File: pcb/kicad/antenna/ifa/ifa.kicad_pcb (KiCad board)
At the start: 2 copper layers, 27.6 x 86.4 mm, 1 part, among them P1 CONN_01X02

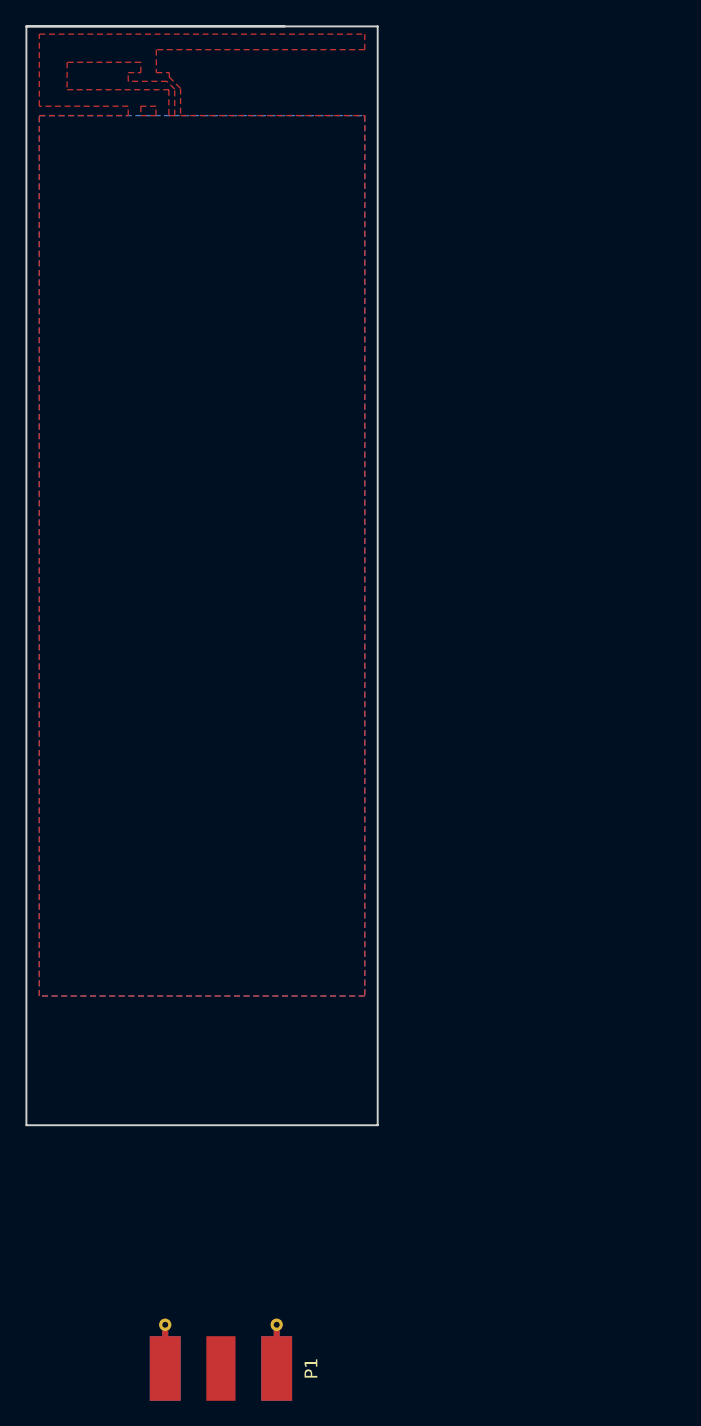
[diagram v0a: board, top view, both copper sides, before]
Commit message: Add second half of initial IFA design
Vias, drills, and padding still need to be configured.
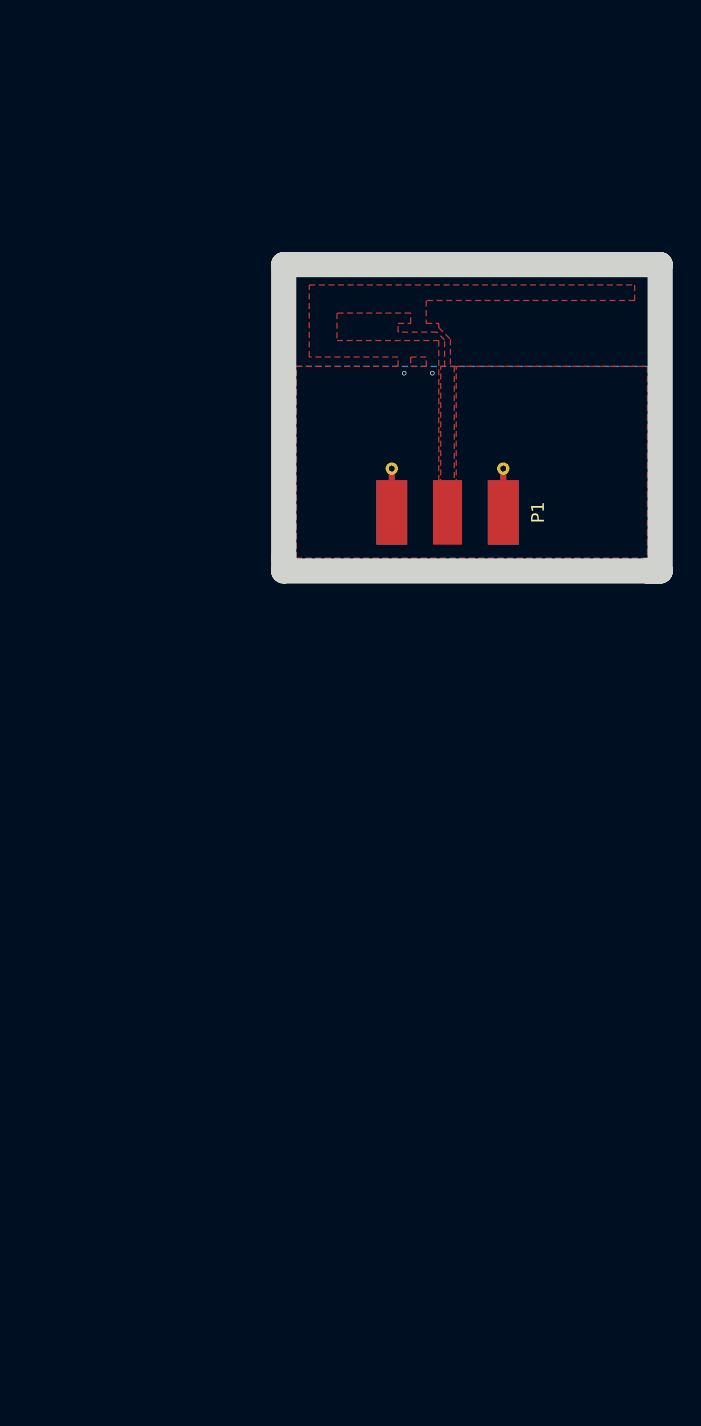
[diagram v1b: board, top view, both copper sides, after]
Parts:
- moved P1 69.6 mm to (142.3, 94.9)
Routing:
- net (no net): vias 0 -> 2
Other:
- board size 27.6 x 86.4 mm -> 29.6 x 24.1 mm
- net class Default: clearance 0.2 -> 0.254; trace_width 0.25 -> 0.127; via_dia 0.6 -> 0.3556; via_drill 0.4 -> 0.254
- rule trace_clearance: 0.2 -> 0.254
- rule trace_min: 0.2 -> 0.127
- rule via_min_drill: 0.3 -> 0.254
- rule via_min_size: 0.4 -> 0.254
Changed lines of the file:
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@@
   (general
     (links 10)
-    (no_connects 6)
-    (area 0 0 0 0)
+    (no_connects 4)
+    (area 107.238799 56.438799 138.811001 82.499201)
     (thickness 1.6)
-    (drawings 9)
-    (tracks 0)
+    (drawings 10)
+    (tracks 2)
     (zones 0)
     (modules 1)
@@
   (layers
     (0 F.Cu signal)
-    (31 B.Cu signal hide)
+    (31 B.Cu signal)
     (32 B.Adhes user)
     (33 F.Adhes user)
@@
   )
   (setup
-    (last_trace_width 0.25)
-    (trace_clearance 0.2)
+    (last_trace_width 0.254)
+    (user_trace_width 0.254)
+    (trace_clearance 0.254)
     (zone_clearance 0.508)
     (zone_45_only no)
-    (trace_min 0.2)
+    (trace_min 0.127)
     (segment_width 0.2)
-    (edge_width 0.15)
-    (via_size 0.6)
-    (via_drill 0.4)
-    (via_min_size 0.4)
-    (via_min_drill 0.3)
+    (edge_width 1.9812)
+    (via_size 0.3556)
+    (via_drill 0.254)
+    (via_min_size 0.254)
+    (via_min_drill 0.254)
     (uvia_size 0.3)
     (uvia_drill 0.1)
@@
     (mod_text_size 1 1)
     (mod_text_width 0.15)
-    (pad_size 1.524 1.524)
-    (pad_drill 0.762)
+    (pad_size 5.08 2.29)
+    (pad_drill 0)
     (pad_to_mask_clearance 0.2)
     (aux_axis_origin 10.16 10.16)
     (visible_elements FFFFFF7F)
     (pcbplotparams
-      (layerselection 0x00030_80000001)
+      (layerselection 0x010f0_80000001)
       (usegerberextensions false)
       (excludeedgelayer true)
@@
       (outputformat 1)
       (mirror false)
-      (drillshape 1)
+      (drillshape 0)
       (scaleselection 1)
       (outputdirectory ""))
@@
   (net 1 GND)
   (net_class Default "This is the default net class."
-    (clearance 0.2)
-    (trace_width 0.25)
-    (via_dia 0.6)
-    (via_drill 0.4)
+    (clearance 0.254)
+    (trace_width 0.127)
+    (via_dia 0.3556)
+    (via_drill 0.254)
     (uvia_dia 0.3)
     (uvia_drill 0.1)
@@
   )
   (module Connectors_Molex:Molex_SMA_Jack_Edge_Mount (layer F.Cu)
-    (at 124.5108 162.179 90)
+    (at 142.3162 94.8944 90)
     (descr "Molex SMA Jack, Edge Mount, http://www.molex.com/pdm_docs/sd/732511150_sd.pdf")
     (tags "sma edge")
@@
     (fp_line (start -5.91 4.76) (end 0.49 4.76) (layer F.Fab) (width 0.1))
     (pad 1 smd rect (at -1.72 0 90) (size 5.08 2.29) (layers F.Cu F.Paste F.Mask)
-      (net 1 GND))
+      (net 1 GND) (zone_connect 0))
     (pad 2 smd rect (at -1.72 -4.38 90) (size 5.08 2.42) (layers F.Cu F.Paste F.Mask)
       (net 1 GND))
@@
       (net 1 GND))
   )
-  (gr_line (start 109.22 58.42) (end 129.54 58.42) (angle 90) (layer Edge.Cuts) (width 0.15))
-  (gr_line (start 109.22 144.78) (end 109.22 58.42) (angle 90) (layer Edge.Cuts) (width 0.15))
-  (gr_line (start 136.8298 144.78) (end 109.22 144.78) (angle 90) (layer Edge.Cuts) (width 0.15))
-  (gr_line (start 136.8298 58.42) (end 136.8298 144.78) (angle 90) (layer Edge.Cuts) (width 0.15))
-  (gr_line (start 109.22 58.42) (end 136.8298 58.42) (angle 90) (layer Edge.Cuts) (width 0.15))
-  (target plus (at 10.16 10.16) (size 5) (width 0.15) (layer Edge.Cuts))
+  (gr_line (start 159.0294 101.219) (end 159.0294 77.1398) (angle 90) (layer Edge.Cuts) (width 1.9812))
+  (gr_line (start 158.0388 101.219) (end 159.0294 101.219) (angle 90) (layer Edge.Cuts) (width 1.9812))
+  (gr_line (start 129.4384 101.219) (end 159.0294 101.219) (angle 90) (layer Edge.Cuts) (width 1.9812))
+  (gr_line (start 129.4384 100.2284) (end 129.4384 101.219) (angle 90) (layer Edge.Cuts) (width 1.9812))
+  (gr_line (start 129.4384 77.1398) (end 129.4384 100.2284) (angle 90) (layer Edge.Cuts) (width 1.9812))
+  (gr_line (start 159.004 77.1398) (end 159.0294 77.1398) (angle 90) (layer Edge.Cuts) (width 1.9812))
+  (gr_line (start 129.4384 77.1398) (end 159.004 77.1398) (angle 90) (layer Edge.Cuts) (width 1.9812))
   (gr_text 0.1 (at 270.51 193.04) (layer Cmts.User)
     (effects (font (size 1.5 1.5) (thickness 0.3)))
@@
     (effects (font (size 1.5 1.5) (thickness 0.3)))
   )
+  (via (at 138.9126 85.6742) (size 0.3556) (drill 0.254) (layers F.Cu B.Cu) (net 0))
+  (via (at 141.1224 85.6742) (size 0.3556) (drill 0.254) (layers F.Cu B.Cu) (net 0))
   (zone (net 1) (net_name GND) (layer F.Cu) (hatch edge 0.508)
+    (connect_pads (clearance 0.254))
+    (min_thickness 0.254)
+    (fill yes (arc_segments 16) (thermal_gap 0.508) (thermal_bridge_width 0.508))
+    (polygon
+      (pts
+        (xy 130.429 85.1408) (xy 138.43 85.1408) (xy 138.43 84.4042) (xy 131.445 84.4042) (xy 131.445 78.74)
+        (xy 157.0228 78.74) (xy 157.0228 79.9592) (xy 140.6398 79.9592) (xy 140.6398 81.7626) (xy 141.6304 81.7626)
+        (xy 141.6304 82.0928) (xy 142.5448 83.0072) (xy 142.5448 85.1408) (xy 142.8496 85.1408) (xy 142.8496 94.4626)
+        (xy 143.002 94.4626) (xy 143.002 85.1408) (xy 158.0388 85.1408) (xy 158.0388 100.2284) (xy 130.429 100.2284)
+      )
+    )
+    (polygon
+      (pts        (xy 133.6294 80.9498) (xy 133.6294 83.1088) (xy 141.6304 83.1088) (xy 141.6304 94.4626) (xy 141.7828 94.4626)
+        (xy 141.7828 85.1408) (xy 142.0876 85.1408) (xy 142.0876 83.058) (xy 141.478 82.4484) (xy 138.43 82.4484)
+        (xy 138.43 81.7626) (xy 139.4206 81.7626) (xy 139.4206 80.9498)
+      )
+    )
+    (polygon
+      (pts        (xy 139.4206 84.4042) (xy 139.4206 85.1408) (xy 140.6398 85.1408) (xy 140.6398 84.4042)
+      )
+    )
+  )
+  (zone (net 1) (net_name GND) (layer B.Cu) (hatch edge 0.508)
     (connect_pads (clearance 0.508))
     (min_thickness 0.254)
@@
     (polygon
       (pts
-        (xy 135.8138 65.4304) (xy 135.8138 134.62) (xy 110.236 134.62) (xy 110.236 65.4304) (xy 117.221 65.4304)
-        (xy 117.221 64.6938) (xy 110.236 64.6938) (xy 110.236 59.0296) (xy 135.8138 59.0296) (xy 135.8138 60.2488)
-        (xy 119.4308 60.2488) (xy 119.4308 62.0522) (xy 120.4468 62.0522) (xy 120.4468 62.4078) (xy 121.3358 63.2968)
-        (xy 121.3358 65.4304)
-      )
-    )
-    (polygon
-      (pts        (xy 112.4204 61.2394) (xy 112.4204 63.3984) (xy 120.4214 63.3984) (xy 120.4214 65.4304) (xy 120.8786 65.4304)
-        (xy 120.8786 63.3476) (xy 120.269 62.738) (xy 117.221 62.738) (xy 117.221 62.0522) (xy 118.2116 62.0522)
-        (xy 118.2116 61.2394)
-      )
-    )
-    (polygon
-      (pts        (xy 118.2116 64.6938) (xy 118.2116 65.4304) (xy 119.4054 65.4304) (xy 119.4054 64.6938)
-      )
-    )
-  )
-  (zone (net 1) (net_name GND) (layer B.Cu) (hatch edge 0.508)
-    (connect_pads (clearance 0.508))
-    (min_thickness 0.254)
-    (fill (arc_segments 16) (thermal_gap 0.508) (thermal_bridge_width 0.508))
-    (polygon
-      (pts
-        (xy 135.8138 134.62) (xy 110.236 134.62) (xy 110.236 65.4304) (xy 135.8138 65.4304) (xy 135.8138 134.62)
-      )
-    )
+        (xy 158.0388 100.2284) (xy 130.429 100.2284) (xy 130.429 85.1408) (xy 158.0388 85.1408)
+      )
+    )

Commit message: Cleanup vias on layout
Layout is essentially complete, but concerned about the lack of physical
connection between SMA signal and antenna feedline. Further attempts,
especially fill, to fix this introduced more problems with the rest of
the layout.
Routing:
- net GND: vias 0 -> 2
- net (no net): vias 2 -> 0
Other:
- board size 29.6 x 24.1 mm -> 30.1 x 24.3 mm
- net class Default: trace_width 0.127 -> 0.254
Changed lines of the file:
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@@
   (general
     (links 10)
-    (no_connects 4)
-    (area 107.238799 56.438799 138.811001 82.499201)
+    (no_connects 3)
+    (area 128.193799 76.149199 272.295714 194.39)
     (thickness 1.6)
-    (drawings 10)
+    (drawings 11)
     (tracks 2)
     (zones 0)
@@
   (setup
     (last_trace_width 0.254)
-    (user_trace_width 0.254)
     (trace_clearance 0.254)
     (zone_clearance 0.508)
-    (zone_45_only no)
+    (zone_45_only yes)
     (trace_min 0.127)
     (segment_width 0.2)
@@
     (via_min_size 0.254)
     (via_min_drill 0.254)
+    (user_via 1.524 1.27)
+    (user_via 1.778 1.016)
+    (user_via 1.778 1.27)
+    (user_via 1.778 1.524)
+    (user_via 2.032 1.27)
     (uvia_size 0.3)
     (uvia_drill 0.1)
@@
     (mod_text_width 0.15)
     (pad_size 5.08 2.29)
-    (pad_drill 0)
+    (pad_drill 0.6)
     (pad_to_mask_clearance 0.2)
-    (aux_axis_origin 10.16 10.16)
-    (visible_elements FFFFFF7F)
+    (aux_axis_origin 130.429 100.2284)
+    (grid_origin 130.429 100.2284)
+    (visible_elements 7FFFFFFF)
     (pcbplotparams
-      (layerselection 0x010f0_80000001)
+      (layerselection 0x030f0_80000001)
       (usegerberextensions false)
       (excludeedgelayer true)
@@
   (net_class Default "This is the default net class."
     (clearance 0.254)
-    (trace_width 0.127)
+    (trace_width 0.254)
     (via_dia 0.3556)
     (via_drill 0.254)
@@
       (net 1 GND))
   )
-  (gr_line (start 159.0294 101.219) (end 159.0294 77.1398) (angle 90) (layer Edge.Cuts) (width 1.9812))
-  (gr_line (start 158.0388 101.219) (end 159.0294 101.219) (angle 90) (layer Edge.Cuts) (width 1.9812))
-  (gr_line (start 129.4384 101.219) (end 159.0294 101.219) (angle 90) (layer Edge.Cuts) (width 1.9812))
-  (gr_line (start 129.4384 100.2284) (end 129.4384 101.219) (angle 90) (layer Edge.Cuts) (width 1.9812))
-  (gr_line (start 129.4384 77.1398) (end 129.4384 100.2284) (angle 90) (layer Edge.Cuts) (width 1.9812))
-  (gr_line (start 159.004 77.1398) (end 159.0294 77.1398) (angle 90) (layer Edge.Cuts) (width 1.9812))
-  (gr_line (start 129.4384 77.1398) (end 159.004 77.1398) (angle 90) (layer Edge.Cuts) (width 1.9812))
+  (gr_line (start 158.0388 78.1304) (end 130.429 78.1304) (layer Margin) (width 0.2))
+  (gr_line (start 158.0388 100.2284) (end 158.0388 78.1304) (layer Margin) (width 0.2))
+  (gr_line (start 130.429 100.2284) (end 158.0388 100.2284) (layer Margin) (width 0.2))
+  (gr_line (start 130.429 78.1304) (end 130.429 100.2284) (layer Margin) (width 0.2))
+  (gr_line (start 129.1844 77.1398) (end 129.1844 101.473) (angle 90) (layer Edge.Cuts) (width 1.9812))
+  (gr_line (start 159.258 101.473) (end 159.258 77.1398) (angle 90) (layer Edge.Cuts) (width 1.9812))
+  (gr_line (start 129.1844 101.473) (end 159.258 101.473) (angle 90) (layer Edge.Cuts) (width 1.9812))
+  (gr_line (start 159.258 77.1398) (end 129.1844 77.1398) (angle 90) (layer Edge.Cuts) (width 1.9812))
   (gr_text 0.1 (at 270.51 193.04) (layer Cmts.User)
     (effects (font (size 1.5 1.5) (thickness 0.3)))
@@
     (effects (font (size 1.5 1.5) (thickness 0.3)))
   )
-  (via (at 138.9126 85.6742) (size 0.3556) (drill 0.254) (layers F.Cu B.Cu) (net 0))
-  (via (at 141.1224 85.6742) (size 0.3556) (drill 0.254) (layers F.Cu B.Cu) (net 0))
+  (via (at 138.9126 85.3948) (size 0.3556) (drill 0.254) (layers F.Cu B.Cu) (net 1))
+  (via (at 141.1224 85.3948) (size 0.3556) (drill 0.254) (layers F.Cu B.Cu) (net 1))
   (zone (net 1) (net_name GND) (layer F.Cu) (hatch edge 0.508)
     (connect_pads (clearance 0.254))

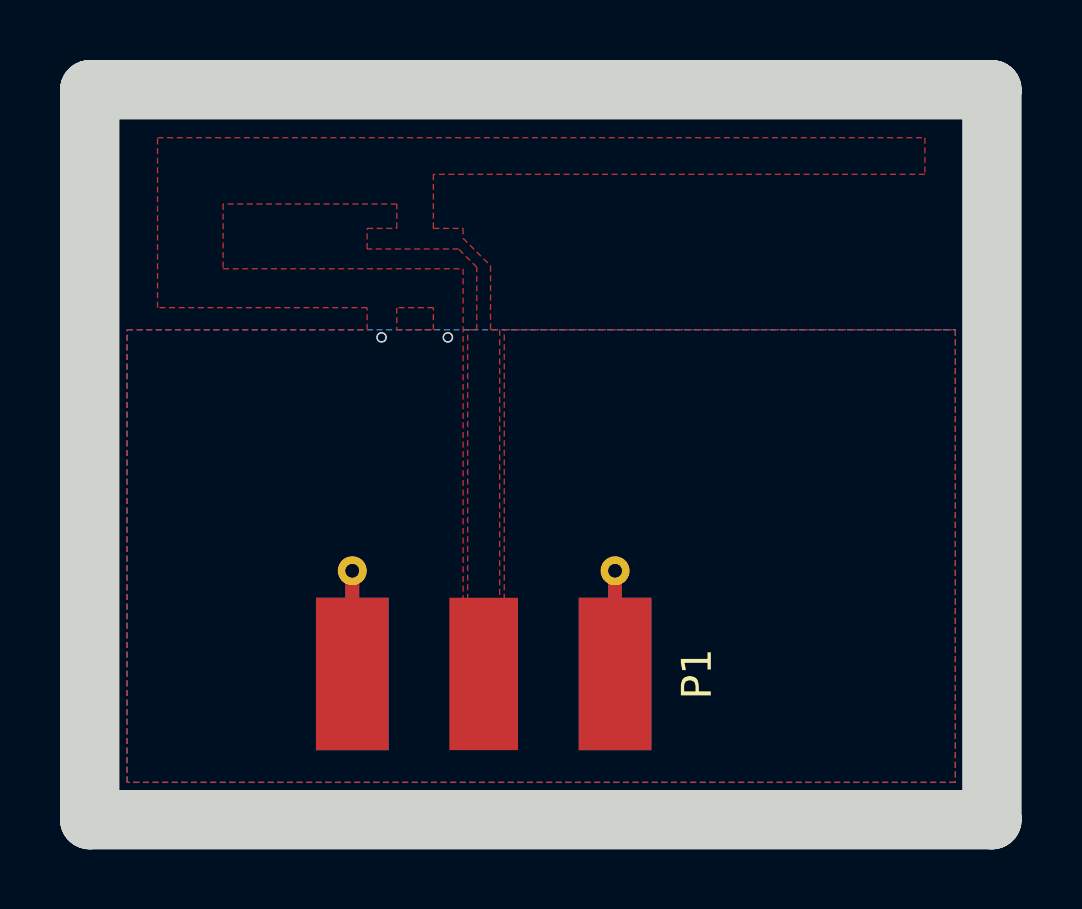
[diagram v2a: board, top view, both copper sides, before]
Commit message: Cleanup copper layer and cut marks
SMA connector now properly connects to the feedline with no breaks. Vias
do not keep their "ground" net if you leave the application and return
at a latter time; workaround has not been found. Extra vias may need to
be placed along the ground plane.
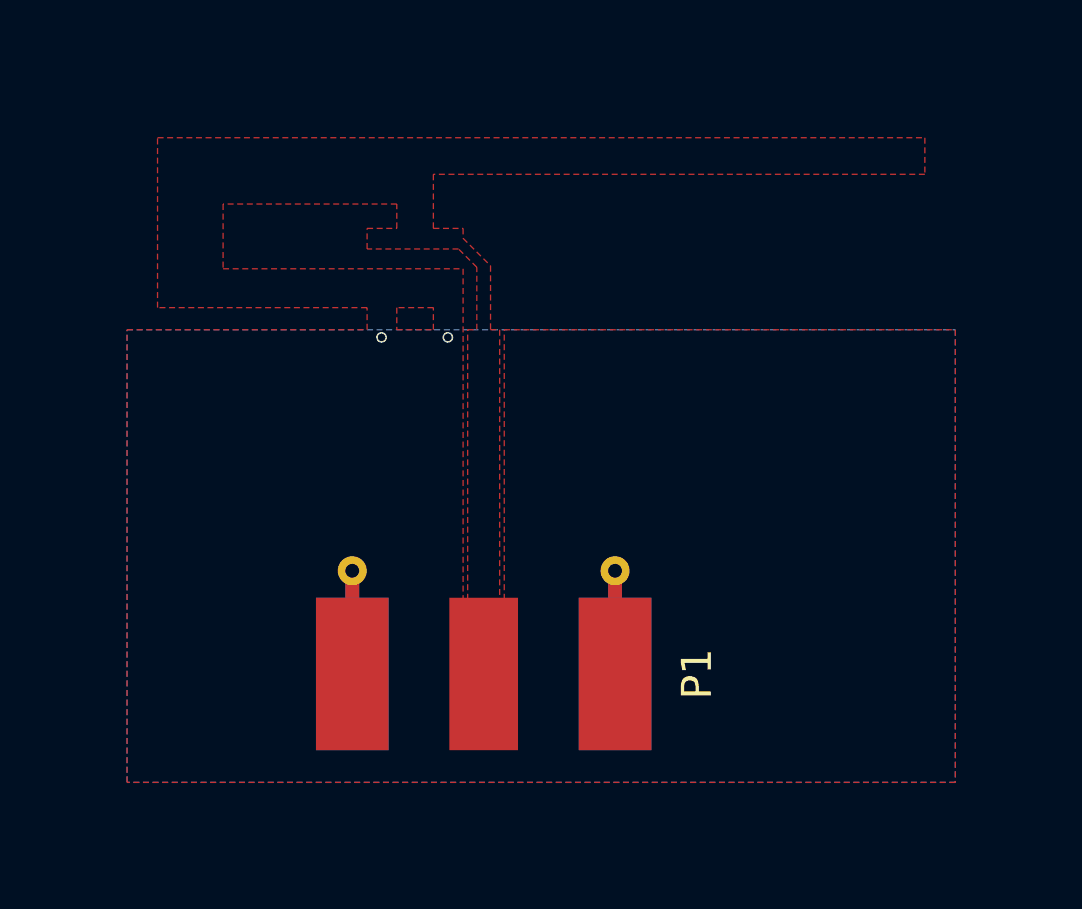
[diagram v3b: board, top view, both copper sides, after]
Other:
- board outline removed
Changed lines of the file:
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@@
   (general
     (links 10)
-    (no_connects 3)
+    (no_connects 2)
     (area 128.193799 76.149199 272.295714 194.39)
     (thickness 1.6)
-    (drawings 11)
+    (drawings 7)
     (tracks 2)
     (zones 0)
@@
     (mod_text_width 0.15)
     (pad_size 5.08 2.29)
-    (pad_drill 0.6)
+    (pad_drill 0)
     (pad_to_mask_clearance 0.2)
     (aux_axis_origin 130.429 100.2284)
@@
     (fp_line (start -5.91 4.76) (end 0.49 4.76) (layer F.Fab) (width 0.1))
     (pad 1 smd rect (at -1.72 0 90) (size 5.08 2.29) (layers F.Cu F.Paste F.Mask)
-      (net 1 GND) (zone_connect 0))
+      (net 1 GND))
     (pad 2 smd rect (at -1.72 -4.38 90) (size 5.08 2.42) (layers F.Cu F.Paste F.Mask)
       (net 1 GND))
@@
       (net 1 GND))
   )
-  (gr_line (start 158.0388 78.1304) (end 130.429 78.1304) (layer Margin) (width 0.2))
-  (gr_line (start 158.0388 100.2284) (end 158.0388 78.1304) (layer Margin) (width 0.2))
-  (gr_line (start 130.429 100.2284) (end 158.0388 100.2284) (layer Margin) (width 0.2))
-  (gr_line (start 130.429 78.1304) (end 130.429 100.2284) (layer Margin) (width 0.2))
-  (gr_line (start 129.1844 77.1398) (end 129.1844 101.473) (angle 90) (layer Edge.Cuts) (width 1.9812))
-  (gr_line (start 159.258 101.473) (end 159.258 77.1398) (angle 90) (layer Edge.Cuts) (width 1.9812))
-  (gr_line (start 129.1844 101.473) (end 159.258 101.473) (angle 90) (layer Edge.Cuts) (width 1.9812))
-  (gr_line (start 159.258 77.1398) (end 129.1844 77.1398) (angle 90) (layer Edge.Cuts) (width 1.9812))
+  (gr_line (start 158.0388 100.2284) (end 130.429 100.2284) (angle 90) (layer Margin) (width 0.2))
+  (gr_line (start 158.0388 78.1304) (end 158.0388 100.2284) (angle 90) (layer Margin) (width 0.2))
+  (gr_line (start 130.429 78.1304) (end 158.0388 78.1304) (angle 90) (layer Margin) (width 0.2))
+  (gr_line (start 130.429 100.2284) (end 130.429 78.1304) (angle 90) (layer Margin) (width 0.2))
   (gr_text 0.1 (at 270.51 193.04) (layer Cmts.User)
     (effects (font (size 1.5 1.5) (thickness 0.3)))
@@
     (effects (font (size 1.5 1.5) (thickness 0.3)))
   )
+  (via (at 141.1224 85.3948) (size 0.3556) (drill 0.254) (layers F.Cu B.Cu) (net 1))
   (via (at 138.9126 85.3948) (size 0.3556) (drill 0.254) (layers F.Cu B.Cu) (net 1))
-  (via (at 141.1224 85.3948) (size 0.3556) (drill 0.254) (layers F.Cu B.Cu) (net 1))
   (zone (net 1) (net_name GND) (layer F.Cu) (hatch edge 0.508)
     (connect_pads (clearance 0.254))
@@
       )
     )
+  )
+  (zone (net 0) (net_name "") (layer F.Cu) (hatch edge 0.508)
+    (connect_pads (clearance 0.508))
+    (min_thickness 0.254)
+    (keepout (tracks not_allowed) (vias not_allowed) (copperpour not_allowed))
+    (fill (arc_segments 16) (thermal_gap 0.508) (thermal_bridge_width 0.508))
+    (polygon
+      (pts
+        (xy 142.0622 96.9518) (xy 142.5702 96.9518) (xy 142.5702 96.266) (xy 143.9672 96.266) (xy 143.9672 96.9518)
+        (xy 142.6464 96.9518) (xy 142.6464 99.6442) (xy 141.986 99.6442) (xy 141.986 96.9518) (xy 140.6652 96.9518)
+        (xy 140.6652 96.266) (xy 142.0622 96.266)
+      )
+    )
